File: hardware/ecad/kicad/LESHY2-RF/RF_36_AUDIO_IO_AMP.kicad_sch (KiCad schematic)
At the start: 0 parts

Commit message: complete exact H2.3.1 RF power hierarchy
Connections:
- no-connect marks 0 -> 7
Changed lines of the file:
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@@
 	(generator_version "10.0")
 	(paper "A4")
+	(hierarchical_label "3V3_MAIN"
+		(shape bidirectional)
+		(at 20.32 20.32 0)
+		(effects (font (size 1.27 1.27)))
+	)
+	(wire
+		(pts (xy 20.32 20.32) (xy 25.40 20.32))
+		(stroke (width 0) (type default))
+	)
+	(no_connect (at 25.40 20.32)
+	)
+	(hierarchical_label "AUDIO_GROUND"
+		(shape bidirectional)
+		(at 20.32 25.40 0)
+		(effects (font (size 1.27 1.27)))
+	)
+	(wire
+		(pts (xy 20.32 25.40) (xy 25.40 25.40))
+		(stroke (width 0) (type default))
+	)
+	(no_connect (at 25.40 25.40)
+	)
+	(hierarchical_label "MIC_RAW"
+		(shape bidirectional)
+		(at 20.32 30.48 0)
+		(effects (font (size 1.27 1.27)))
+	)
+	(wire
+		(pts (xy 20.32 30.48) (xy 25.40 30.48))
+		(stroke (width 0) (type default))
+	)
+	(no_connect (at 25.40 30.48)
+	)
+	(hierarchical_label "POWER_GROUND"
+		(shape bidirectional)
+		(at 20.32 35.56 0)
+		(effects (font (size 1.27 1.27)))
+	)
+	(wire
+		(pts (xy 20.32 35.56) (xy 25.40 35.56))
+		(stroke (width 0) (type default))
+	)
+	(no_connect (at 25.40 35.56)
+	)
+	(hierarchical_label "SPEAKER_AMP_EN"
+		(shape bidirectional)
+		(at 190.50 20.32 180)
+		(effects (font (size 1.27 1.27)) (justify right))
+	)
+	(wire
+		(pts (xy 190.50 20.32) (xy 185.42 20.32))
+		(stroke (width 0) (type default))
+	)
+	(no_connect (at 185.42 20.32)
+	)
+	(hierarchical_label "SPEAKER_SELECTED_N"
+		(shape bidirectional)
+		(at 190.50 25.40 180)
+		(effects (font (size 1.27 1.27)) (justify right))
+	)
+	(wire
+		(pts (xy 190.50 25.40) (xy 185.42 25.40))
+		(stroke (width 0) (type default))
+	)
+	(no_connect (at 185.42 25.40)
+	)
+	(hierarchical_label "SPEAKER_SELECTED_P"
+		(shape bidirectional)
+		(at 190.50 30.48 180)
+		(effects (font (size 1.27 1.27)) (justify right))
+	)
+	(wire
+		(pts (xy 190.50 30.48) (xy 185.42 30.48))
+		(stroke (width 0) (type default))
+	)
+	(no_connect (at 185.42 30.48)
+	)
 	(sheet_instances
 		(path "/"

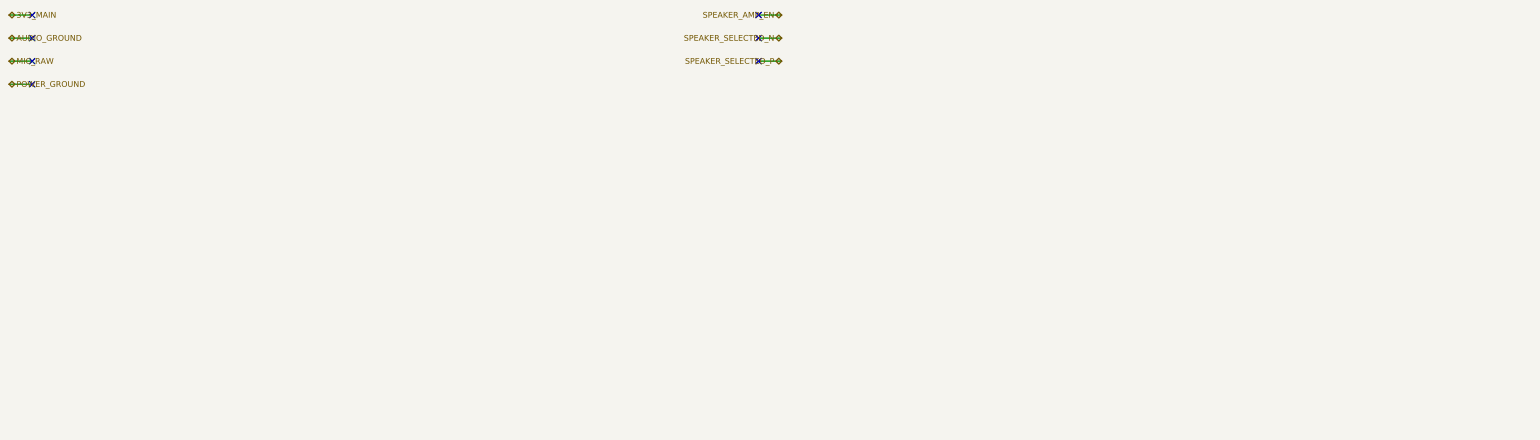
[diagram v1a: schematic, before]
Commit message: complete exact H2.3.10 audio IO sheet
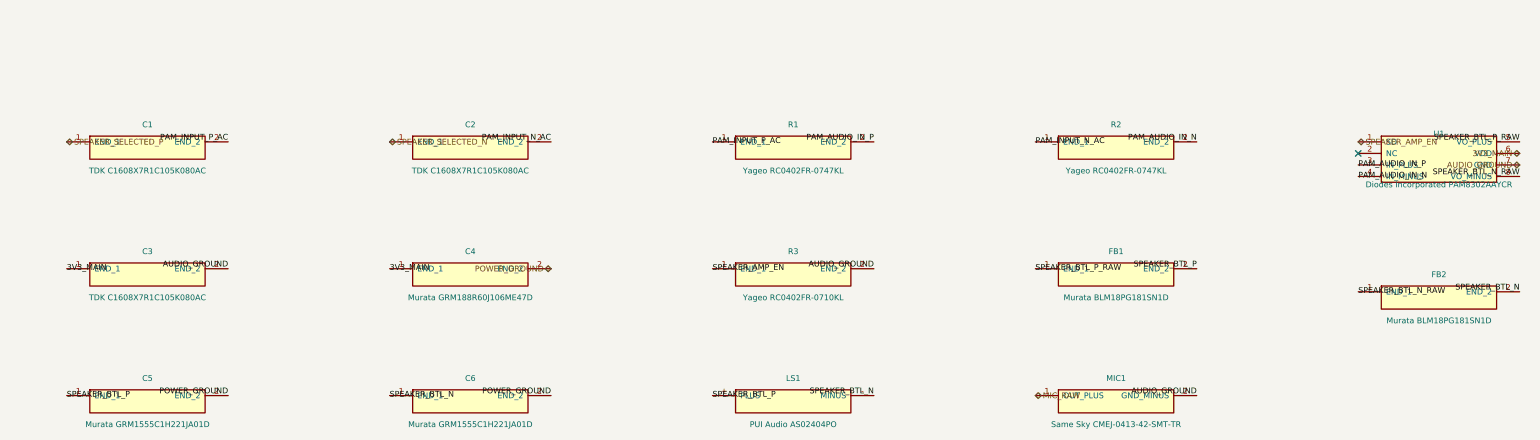
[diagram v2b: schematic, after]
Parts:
- added C1: TDK C1608X7R1C105K080AC, Capacitor_SMD:C_0603_1608Metric, symbol Leshy2:RF36_SPEAKER_INPUT_P_COUPLING
- added C2: TDK C1608X7R1C105K080AC, Capacitor_SMD:C_0603_1608Metric, symbol Leshy2:RF36_SPEAKER_INPUT_N_COUPLING
- added C3: TDK C1608X7R1C105K080AC, Capacitor_SMD:C_0603_1608Metric, symbol Leshy2:RF36_SPEAKER_AMP_INPUT_CAP
- added C4: Murata GRM188R60J106ME47D, Capacitor_SMD:C_0603_1608Metric, symbol Leshy2:RF36_SPEAKER_AMP_BULK_CAP
- added C5: Murata GRM1555C1H221JA01D, Capacitor_SMD:C_0402_1005Metric, symbol Leshy2:RF36_SPEAKER_OUTPUT_CAP_P
- added C6: Murata GRM1555C1H221JA01D, Capacitor_SMD:C_0402_1005Metric, symbol Leshy2:RF36_SPEAKER_OUTPUT_CAP_N
- added FB1: Murata BLM18PG181SN1D, Inductor_SMD:L_0603_1608Metric, symbol Leshy2:RF36_SPEAKER_OUTPUT_BEAD_P
- added FB2: Murata BLM18PG181SN1D, Inductor_SMD:L_0603_1608Metric, symbol Leshy2:RF36_SPEAKER_OUTPUT_BEAD_N
- added LS1: PUI Audio AS02404PO, Leshy2:Speaker-Wire-Termination-2P, symbol Leshy2:RF36_SPEAKER
- added MIC1: Same Sky CMEJ-0413-42-SMT-TR, Leshy2:CMEJ-0413-42-SMT-TR, symbol Leshy2:RF36_MICROPHONE
- added R1: Yageo RC0402FR-0747KL, Resistor_SMD:R_0402_1005Metric, symbol Leshy2:RF36_SPEAKER_INPUT_P_GAIN
- added R2: Yageo RC0402FR-0747KL, Resistor_SMD:R_0402_1005Metric, symbol Leshy2:RF36_SPEAKER_INPUT_N_GAIN
- added R3: Yageo RC0402FR-0710KL, Resistor_SMD:R_0402_1005Metric, symbol Leshy2:RF36_SPEAKER_AMP_ENABLE_PULLDOWN
- added U1: Diodes Incorporated PAM8302AAYCR, Leshy2:PAM8302AAYCR-UDFN3030-8E, symbol Leshy2:RF36_SPEAKER_AMP
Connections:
- net 3V3_MAIN: now also C3.1 (END_1), C4.1 (END_1), U1.6 (VDD)
- net AUDIO_GROUND: now also C3.2 (END_2), MIC1.2 (GND_MINUS), R3.2 (END_2), U1.7 (GND)
- net MIC_RAW: now also MIC1.1 (OUT_PLUS)
- net POWER_GROUND: now also C4.2 (END_2), C5.2 (END_2), C6.2 (END_2)
- net SPEAKER_AMP_EN: now also R3.1 (END_1), U1.1 (SD)
- net SPEAKER_SELECTED_N: now also C2.1 (END_1)
- net SPEAKER_SELECTED_P: now also C1.1 (END_1)
- new net PAM_AUDIO_IN_N: R2.2 (END_2), U1.4 (IN_MINUS)
- new net PAM_AUDIO_IN_P: R1.2 (END_2), U1.3 (IN_PLUS)
- new net PAM_INPUT_N_AC: C2.2 (END_2), R2.1 (END_1)
- new net PAM_INPUT_P_AC: C1.2 (END_2), R1.1 (END_1)
- new net SPEAKER_BTL_N: C6.1 (END_1), FB2.2 (END_2), LS1.- (MINUS)
- new net SPEAKER_BTL_N_RAW: FB2.1 (END_1), U1.8 (VO_MINUS)
- new net SPEAKER_BTL_P: C5.1 (END_1), FB1.2 (END_2), LS1.+ (PLUS)
- new net SPEAKER_BTL_P_RAW: FB1.1 (END_1), U1.5 (VO_PLUS)
- no-connect marks 7 -> 1
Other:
- title: (none) -> Leshy2 — microphone, reset-safe differential amplifier and wired speaker

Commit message: complete H2 schematic review package
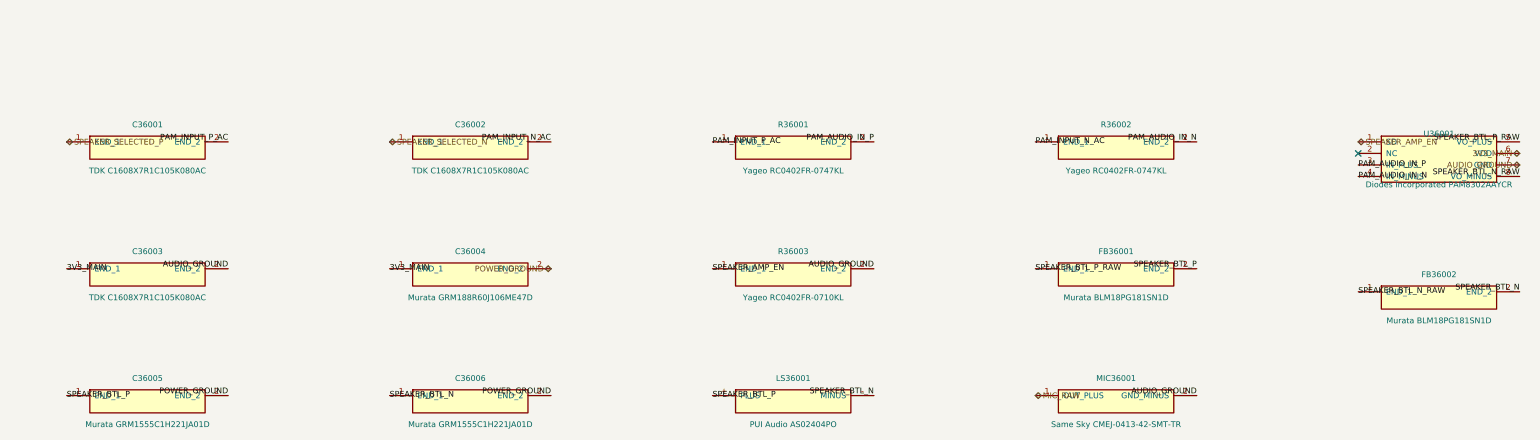
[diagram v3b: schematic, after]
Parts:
- renumbered C1 to C36001, C2 to C36002, C3 to C36003, C4 to C36004, C5 to C36005, C6 to C36006, FB1 to FB36001, FB2 to FB36002, LS1 to LS36001, MIC1 to MIC36001, R1 to R36001, R2 to R36002, R3 to R36003, U1 to U36001
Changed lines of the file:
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@@
 		(on_board yes)
 		(dnp no)
-		(property "Reference" "C1"
+		(property "Reference" "C36001"
 			(at 50.80 44.45 0)
 			(show_name no)
@@
 			(project "LESHY2-RF"
 				(path "/dbfe95ab-2830-5c1b-9bb6-e0e4964eeac0"
-					(reference "C1")
+					(reference "C36001")
 					(unit 1)
 				)
@@
 		(on_board yes)
 		(dnp no)
-		(property "Reference" "C2"
+		(property "Reference" "C36002"
 			(at 121.92 44.45 0)
 			(show_name no)
@@
 			(project "LESHY2-RF"
 				(path "/dbfe95ab-2830-5c1b-9bb6-e0e4964eeac0"
-					(reference "C2")
+					(reference "C36002")
 					(unit 1)
 				)
@@
 		(on_board yes)
 		(dnp no)
-		(property "Reference" "R1"
+		(property "Reference" "R36001"
 			(at 193.04 44.45 0)
 			(show_name no)
@@
 			(project "LESHY2-RF"
 				(path "/dbfe95ab-2830-5c1b-9bb6-e0e4964eeac0"
-					(reference "R1")
+					(reference "R36001")
 					(unit 1)
 				)
@@
 		(on_board yes)
 		(dnp no)
-		(property "Reference" "R2"
+		(property "Reference" "R36002"
 			(at 264.16 44.45 0)
 			(show_name no)
@@
 			(project "LESHY2-RF"
 				(path "/dbfe95ab-2830-5c1b-9bb6-e0e4964eeac0"
-					(reference "R2")
+					(reference "R36002")
 					(unit 1)
 				)
@@
 		(on_board yes)
 		(dnp no)
-		(property "Reference" "U1"
+		(property "Reference" "U36001"
 			(at 335.28 46.47 0)
 			(show_name no)
@@
 			(project "LESHY2-RF"
 				(path "/dbfe95ab-2830-5c1b-9bb6-e0e4964eeac0"
-					(reference "U1")
+					(reference "U36001")
 					(unit 1)
 				)
@@
 		(on_board yes)
 		(dnp no)
-		(property "Reference" "C3"
+		(property "Reference" "C36003"
 			(at 50.80 72.39 0)
 			(show_name no)
@@
 			(project "LESHY2-RF"
 				(path "/dbfe95ab-2830-5c1b-9bb6-e0e4964eeac0"
-					(reference "C3")
+					(reference "C36003")
 					(unit 1)
 				)
@@
 		(on_board yes)
 		(dnp no)
-		(property "Reference" "C4"
+		(property "Reference" "C36004"
 			(at 121.92 72.39 0)
 			(show_name no)
@@
 			(project "LESHY2-RF"
 				(path "/dbfe95ab-2830-5c1b-9bb6-e0e4964eeac0"
-					(reference "C4")
+					(reference "C36004")
 					(unit 1)
 				)
@@
 		(on_board yes)
 		(dnp no)
-		(property "Reference" "R3"
+		(property "Reference" "R36003"
 			(at 193.04 72.39 0)
 			(show_name no)
@@
 			(project "LESHY2-RF"
 				(path "/dbfe95ab-2830-5c1b-9bb6-e0e4964eeac0"
-					(reference "R3")
+					(reference "R36003")
 					(unit 1)
 				)
@@
 		(on_board yes)
 		(dnp no)
-		(property "Reference" "FB1"
+		(property "Reference" "FB36001"
 			(at 264.16 72.39 0)
 			(show_name no)
@@
 			(project "LESHY2-RF"
 				(path "/dbfe95ab-2830-5c1b-9bb6-e0e4964eeac0"
-					(reference "FB1")
+					(reference "FB36001")
 					(unit 1)
 				)
@@
 		(on_board yes)
 		(dnp no)
-		(property "Reference" "FB2"
+		(property "Reference" "FB36002"
 			(at 335.28 77.47 0)
 			(show_name no)
@@
 			(project "LESHY2-RF"
 				(path "/dbfe95ab-2830-5c1b-9bb6-e0e4964eeac0"
-					(reference "FB2")
+					(reference "FB36002")
 					(unit 1)
 				)
@@
 		(on_board yes)
 		(dnp no)
-		(property "Reference" "C5"
+		(property "Reference" "C36005"
 			(at 50.80 100.33 0)
 			(show_name no)
@@
 			(project "LESHY2-RF"
 				(path "/dbfe95ab-2830-5c1b-9bb6-e0e4964eeac0"
-					(reference "C5")
+					(reference "C36005")
 					(unit 1)
 				)
@@
 		(on_board yes)
 		(dnp no)
-		(property "Reference" "C6"
+		(property "Reference" "C36006"
 			(at 121.92 100.33 0)
 			(show_name no)
@@
 			(project "LESHY2-RF"
 				(path "/dbfe95ab-2830-5c1b-9bb6-e0e4964eeac0"
-					(reference "C6")
+					(reference "C36006")
 					(unit 1)
 				)
@@
 		(on_board yes)
 		(dnp no)
-		(property "Reference" "LS1"
+		(property "Reference" "LS36001"
 			(at 193.04 100.33 0)
 			(show_name no)
@@
 			(project "LESHY2-RF"
 				(path "/dbfe95ab-2830-5c1b-9bb6-e0e4964eeac0"
-					(reference "LS1")
+					(reference "LS36001")
 					(unit 1)
 				)
@@
 		(on_board yes)
 		(dnp no)
-		(property "Reference" "MIC1"
+		(property "Reference" "MIC36001"
 			(at 264.16 100.33 0)
 			(show_name no)
@@
 			(project "LESHY2-RF"
 				(path "/dbfe95ab-2830-5c1b-9bb6-e0e4964eeac0"
-					(reference "MIC1")
-					(unit 1)
-				)
+					(reference "MIC36001")
+					(unit 1)
+				)
